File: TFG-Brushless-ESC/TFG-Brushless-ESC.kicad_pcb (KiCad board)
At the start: 4 copper layers, 124.9 x 44 mm, 179 parts, among them J2 USB C Receptacle, J3 HALL SENSORS, J4 SWD-I2C, J5 24V IN, Q1 TK58E06N1, Q2 TK58E06N1, Q3 TK58E06N1, Q4 TK58E06N1, Q5 TK58E06N1, Q6 TK58E06N1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

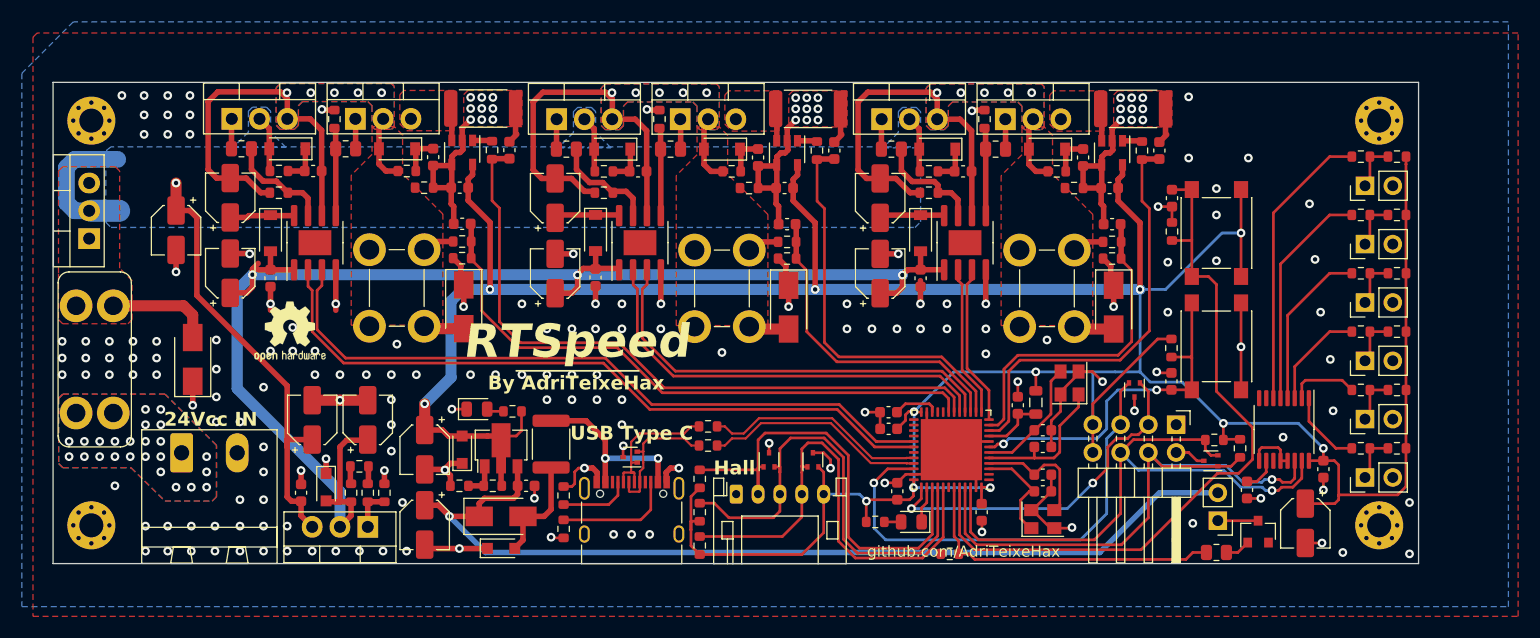
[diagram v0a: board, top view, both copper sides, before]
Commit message: minor pcb fixes and start of analog implementation
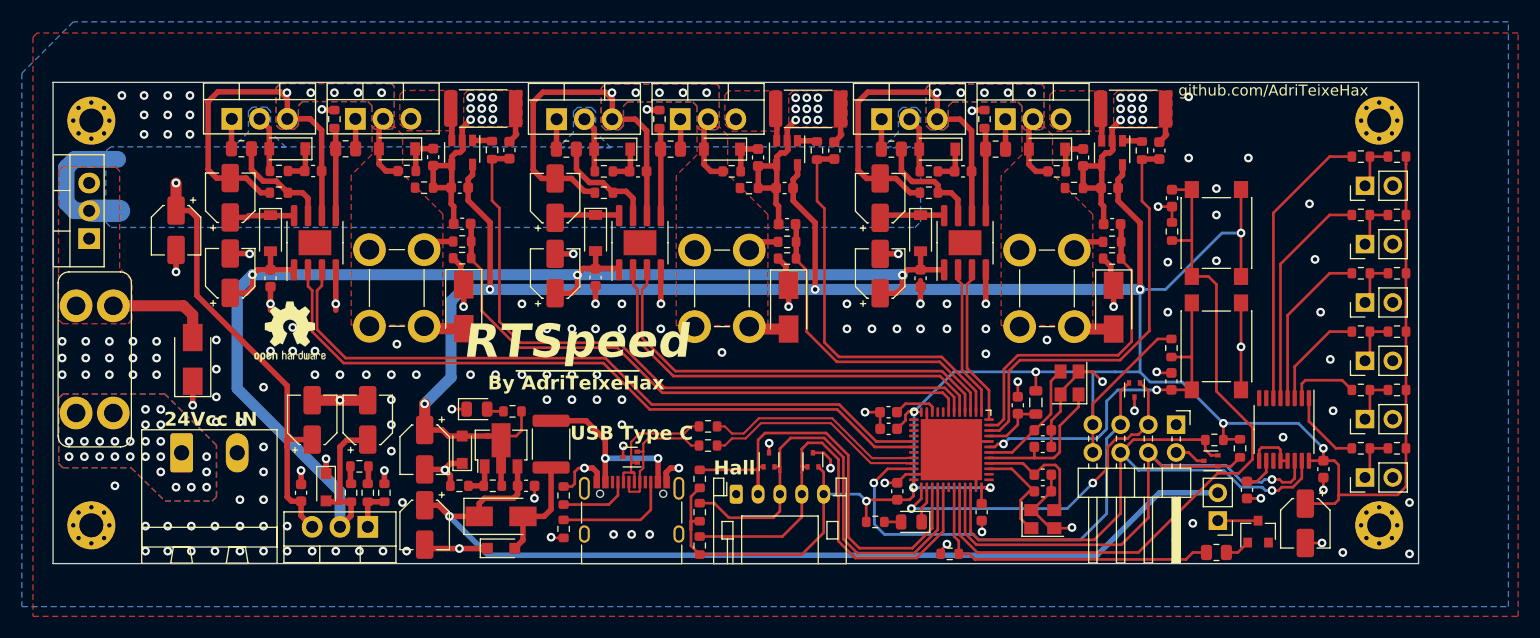
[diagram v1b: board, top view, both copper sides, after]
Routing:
- net GND: track 207.2 -> 208.4 mm, vias 193 -> 194
- net +12V: track 128.1 -> 127.6 mm
